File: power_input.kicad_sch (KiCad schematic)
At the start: 112 parts, among them J201 61300211121, J202 61300211121, J203 61300211121, J204 61300211121, J205 61300211121, J206 61300211121, J207 61300211121, J208 61300211121, Q201 DMPH4029LFGQ, Q202 DMPH4029LFGQ, Q203 IRFL4315PbF, Q204 DMPH4029LFGQ, Q205 DMPH4029LFGQ, U201 LM4040-5.0, U202 TL331, U203 OPA197, U204 LM4040-5.0, U205 TL331, U206 LM4040-5.0, U207 TL331

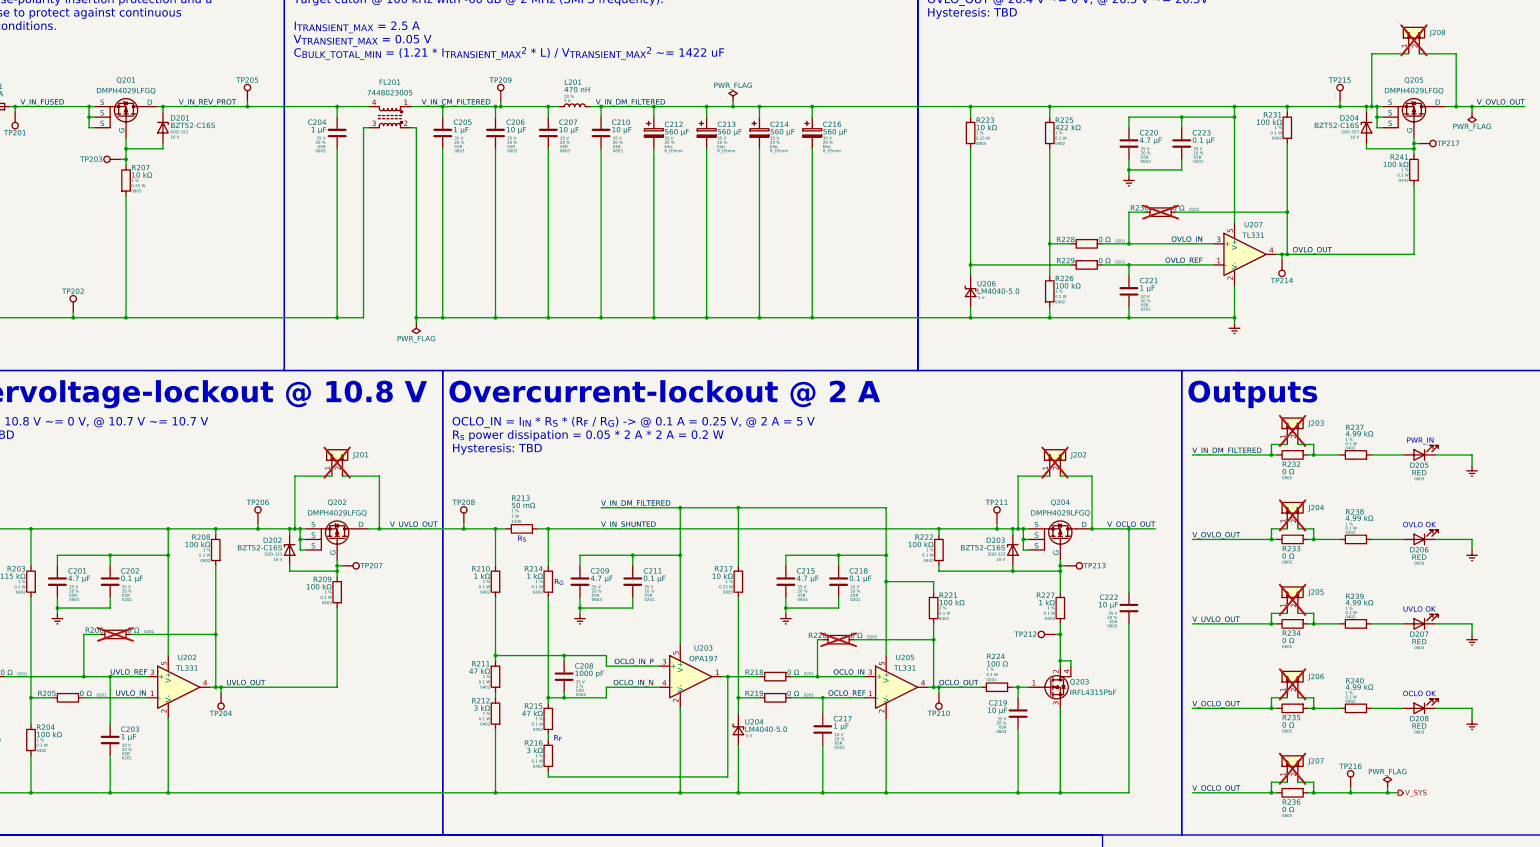
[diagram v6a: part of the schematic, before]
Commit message: Remove redundant test points and add bottom silkscreen
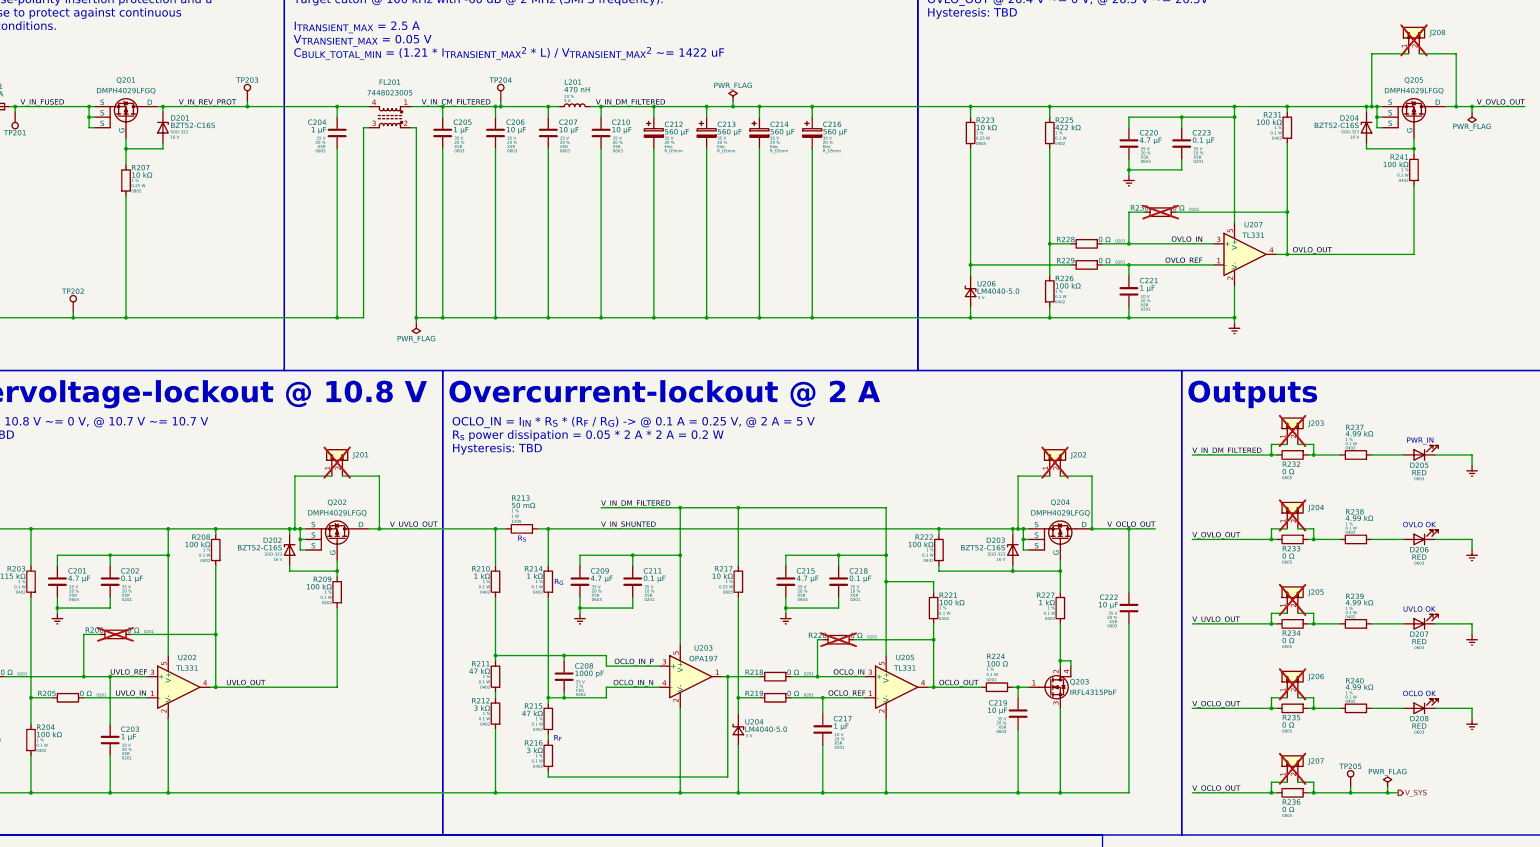
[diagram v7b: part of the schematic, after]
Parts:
- removed TP203, TP204, TP206, TP207, TP208, TP210, TP211, TP212, TP213, TP214, TP215, TP217: TestPoint, TestPoint:TestPoint_Pad_D1.0mm, symbol Connector:TestPoint
- renumbered TP205 to TP203, TP209 to TP204, TP216 to TP205
